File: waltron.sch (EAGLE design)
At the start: 21 parts, among them IC1 4049N, U1 LM386

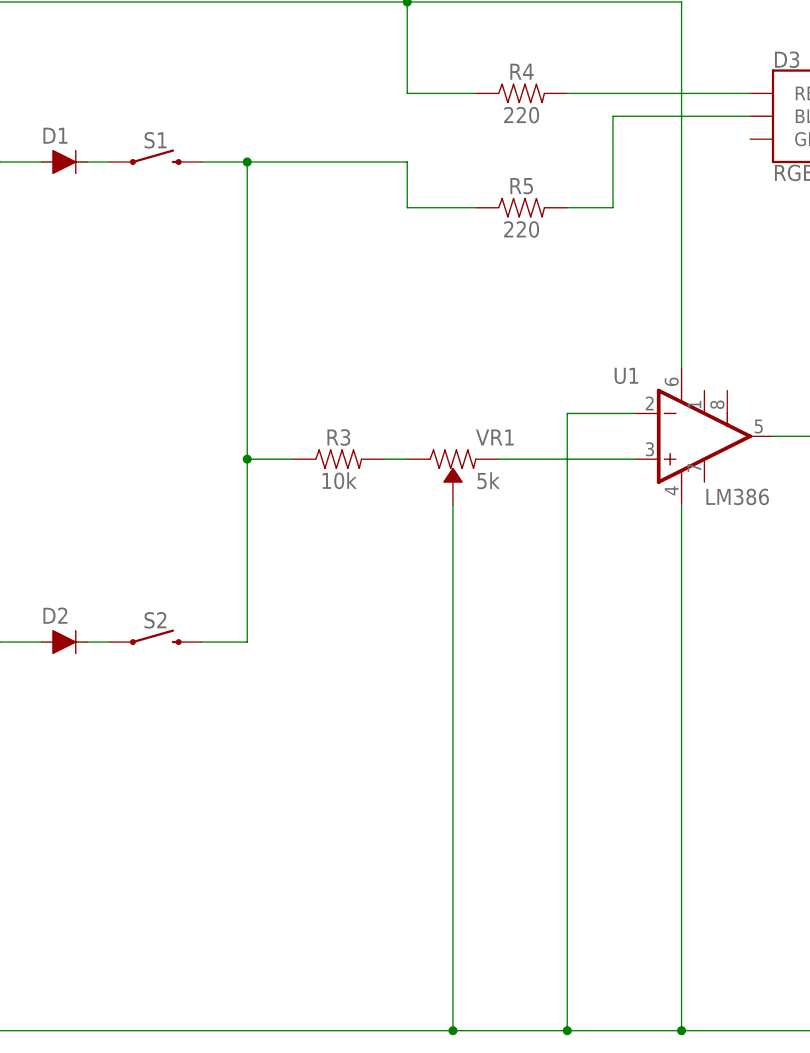
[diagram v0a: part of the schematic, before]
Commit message: Fix miswired volume pot
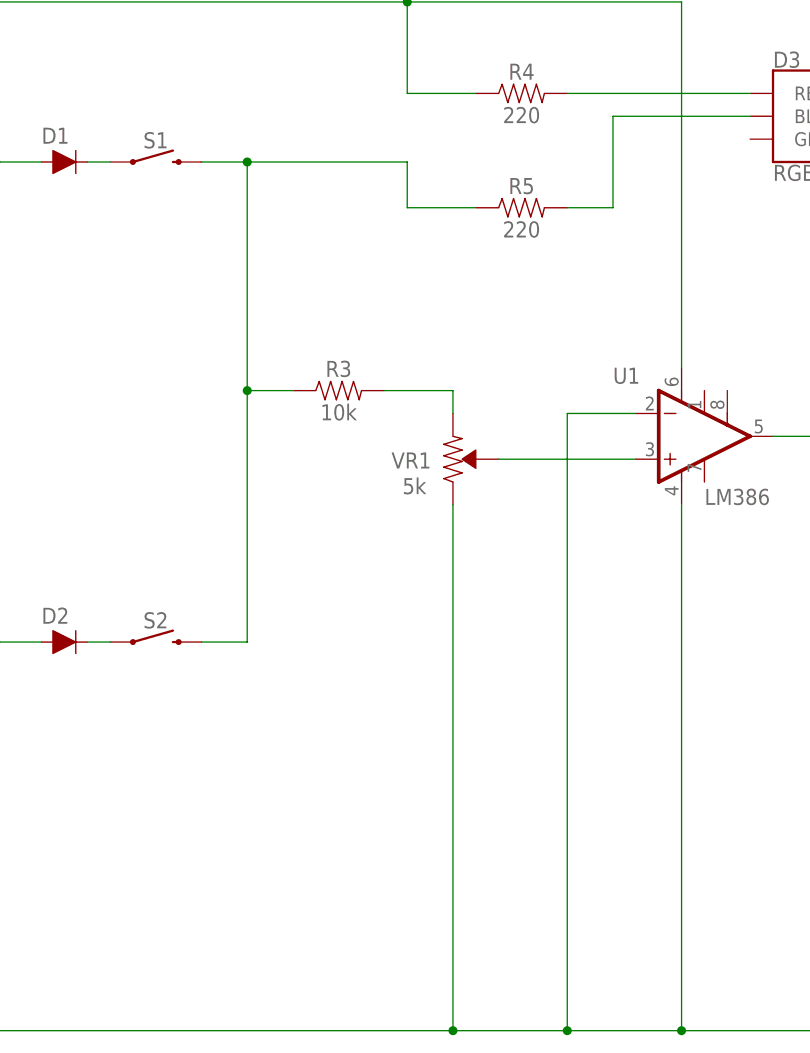
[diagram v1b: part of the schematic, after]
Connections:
- net GND: now also VR1.CW; no longer VR1.WIPER
- net N$13: now also R3.2; no longer U1.+IN
- net N$16: now also U1.+IN, VR1.WIPER; no longer R3.2, VR1.CW
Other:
- moved on the sheet: R3, VR1
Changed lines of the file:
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@@
 <attribute name="VALUE" x="104.14" y="14.732" size="1.778" layer="96" font="vector" align="top-center"/>
 </instance>
-<instance part="VR1" gate="R?" x="137.16" y="35.56" rot="R270"/>
+<instance part="VR1" gate="R?" x="137.16" y="35.56" smashed="yes">
+<attribute name="NAME" x="134.7417625" y="36.30701875" size="1.778" layer="95" font="vector" rot="R180"/>
+<attribute name="VALUE" x="134.206484375" y="31.675228125" size="1.778" layer="96" font="vector" rot="R180" align="top-left"/>
+</instance>
 <instance part="U1" gate="G1" x="162.56" y="38.1" smashed="yes">
 <attribute name="NAME" x="154.94" y="43.942" size="1.778" layer="95" font="vector"/>
@@
 <instance part="R5" gate="G$1" x="144.78" y="63.5"/>
 <instance part="R4" gate="G$1" x="144.78" y="76.2"/>
-<instance part="R3" gate="G$1" x="124.46" y="35.56"/>
+<instance part="R3" gate="G$1" x="124.46" y="43.18"/>
 <instance part="D1" gate="G$1" x="93.98" y="68.58"/>
 <instance part="D2" gate="G$1" x="93.98" y="15.24"/>
@@
 <net name="N$12" class="0">
 <segment>
-<wire x1="114.3" y1="68.58" x2="114.3" y2="35.56" width="0.1524" layer="91"/>
-<wire x1="114.3" y1="35.56" x2="114.3" y2="15.24" width="0.1524" layer="91"/>
+<wire x1="114.3" y1="68.58" x2="114.3" y2="43.18" width="0.1524" layer="91"/>
+<wire x1="114.3" y1="43.18" x2="114.3" y2="15.24" width="0.1524" layer="91"/>
 <pinref part="S1" gate="G$1" pin="2"/>
 <wire x1="109.22" y1="68.58" x2="114.3" y2="68.58" width="0.1524" layer="91"/>
@@
 <wire x1="109.22" y1="15.24" x2="114.3" y2="15.24" width="0.1524" layer="91"/>
 <pinref part="R3" gate="G$1" pin="1"/>
-<wire x1="119.38" y1="35.56" x2="114.3" y2="35.56" width="0.1524" layer="91"/>
-<junction x="114.3" y="35.56"/>
+<wire x1="119.38" y1="43.18" x2="114.3" y2="43.18" width="0.1524" layer="91"/>
+<junction x="114.3" y="43.18"/>
 <wire x1="114.3" y1="68.58" x2="132.08" y2="68.58" width="0.1524" layer="91"/>
 <junction x="114.3" y="68.58"/>
@@
 </segment>
 </net>
-<net name="N$13" class="0">
-<segment>
-<pinref part="VR1" gate="R?" pin="CCW"/>
-<pinref part="U1" gate="G1" pin="+IN"/>
-<wire x1="142.24" y1="35.56" x2="157.48" y2="35.56" width="0.1524" layer="91"/>
-</segment>
-</net>
 <net name="N$14" class="0">
 <segment>
@@
 <pinref part="S2" gate="G$1" pin="1"/>
 <wire x1="96.52" y1="15.24" x2="99.06" y2="15.24" width="0.1524" layer="91"/>
-</segment>
-</net>
-<net name="N$16" class="0">
-<segment>
-<pinref part="R3" gate="G$1" pin="2"/>
-<pinref part="VR1" gate="R?" pin="CW"/>
-<wire x1="129.54" y1="35.56" x2="132.08" y2="35.56" width="0.1524" layer="91"/>
 </segment>
 </net>
@@
 <net name="GND" class="1">
 <segment>
-<pinref part="VR1" gate="R?" pin="WIPER"/>
-<wire x1="137.16" y1="30.48" x2="137.16" y2="-27.94" width="0.1524" layer="91"/>
 <pinref part="U1" gate="G1" pin="-IN"/>
 <wire x1="157.48" y1="40.64" x2="149.86" y2="40.64" width="0.1524" layer="91"/>
 <wire x1="149.86" y1="40.64" x2="149.86" y2="-27.94" width="0.1524" layer="91"/>
-<wire x1="149.86" y1="-27.94" x2="137.16" y2="-27.94" width="0.1524" layer="91"/>
 <pinref part="U1" gate="G1" pin="V-"/>
 <wire x1="162.56" y1="30.48" x2="162.56" y2="-27.94" width="0.1524" layer="91"/>
@@
 <wire x1="-40.64" y1="35.56" x2="-40.64" y2="-27.94" width="0.1524" layer="91"/>
 <wire x1="-40.64" y1="-27.94" x2="-27.94" y2="-27.94" width="0.1524" layer="91"/>
-<junction x="137.16" y="-27.94"/>
 <wire x1="-27.94" y1="-27.94" x2="137.16" y2="-27.94" width="0.1524" layer="91"/>
+<wire x1="137.16" y1="-27.94" x2="149.86" y2="-27.94" width="0.1524" layer="91"/>
 <wire x1="-27.94" y1="27.94" x2="-27.94" y2="-27.94" width="0.1524" layer="91"/>
 <junction x="-27.94" y="-27.94"/>
@@
 <wire x1="-20.32" y1="33.02" x2="-20.32" y2="27.94" width="0.1524" layer="91"/>
 <wire x1="-20.32" y1="27.94" x2="-27.94" y2="27.94" width="0.1524" layer="91"/>
-</segment>
-</net>
+<pinref part="VR1" gate="R?" pin="CW"/>
+<wire x1="137.16" y1="30.48" x2="137.16" y2="-27.94" width="0.1524" layer="91"/>
+<junction x="137.16" y="-27.94"/>
+</segment>
+</net>
+<net name="N$13" class="0">
+<segment>
+<pinref part="R3" gate="G$1" pin="2"/>
+<wire x1="129.54" y1="43.18" x2="137.16" y2="43.18" width="0.1524" layer="91"/>
+<pinref part="VR1" gate="R?" pin="CCW"/>
+<wire x1="137.16" y1="43.18" x2="137.16" y2="40.64" width="0.1524" layer="91"/>
+</segment>
+</net>
+<net name="N$16" class="0">
+<segment>
+<pinref part="VR1" gate="R?" pin="WIPER"/>
+<pinref part="U1" gate="G1" pin="+IN"/>
+<wire x1="142.24" y1="35.56" x2="157.48" y2="35.56" width="0.1524" layer="91"/>
+</segment>
+</net>

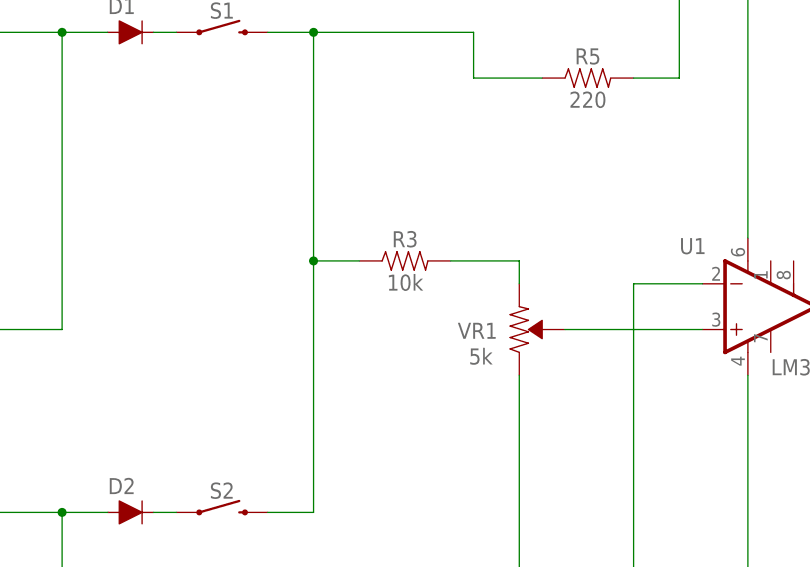
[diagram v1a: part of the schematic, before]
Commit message: Lay resistors flat, rip up routes
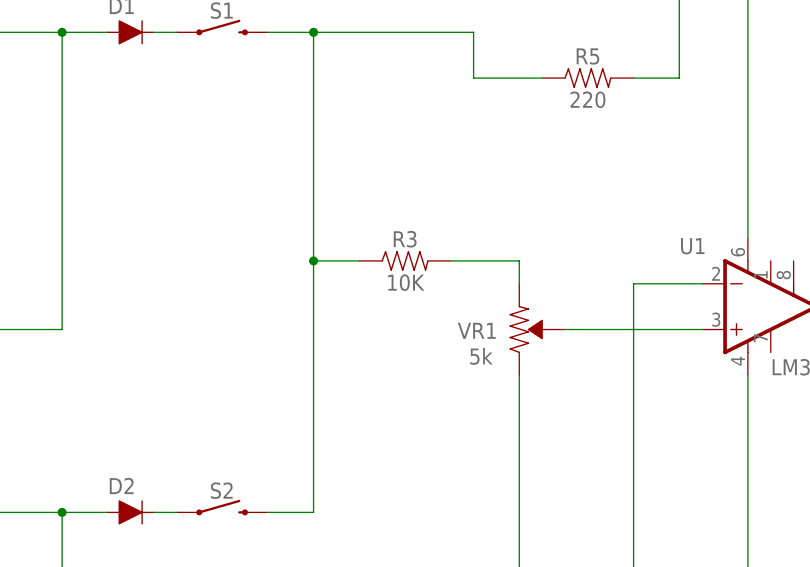
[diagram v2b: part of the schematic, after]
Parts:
- R1, R2, R4, R5: device SparkFun-Resistors:1MOHM-VERT-1/4W-5% -> SparkFun-Resistors:1KOHM-HORIZ-1/4W-1%
- R3: value 10k -> 10K; device SparkFun-Resistors:1MOHM-VERT-1/4W-5% -> SparkFun-Resistors:1KOHM-HORIZ-1/4W-1%
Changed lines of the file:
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@@
 <part name="PR1" library="SparkFun-Sensors" deviceset="PHOTOCELL" device="PTH-KIT" value=""/>
 <part name="C2" library="SparkFun-Capacitors" deviceset="10UF-POLAR" device="-RADIAL-2.5MM-25V-20%" value="4.7uF"/>
-<part name="R1" library="SparkFun-Resistors" deviceset="1MOHM" device="-VERT-1/4W-5%" value="1M"/>
+<part name="R1" library="SparkFun-Resistors" deviceset="1KOHM" device="-HORIZ-1/4W-1%" value="1M"/>
 <part name="S1" library="SparkFun-Switches" deviceset="MOMENTARY-SWITCH-SPST" device="-PTH-6.0MM" value=""/>
-<part name="R2" library="SparkFun-Resistors" deviceset="1MOHM" device="-VERT-1/4W-5%" value="1M"/>
+<part name="R2" library="SparkFun-Resistors" deviceset="1KOHM" device="-HORIZ-1/4W-1%" value="1M"/>
 <part name="C1" library="SparkFun-Capacitors" deviceset="0.1UF" device="-KIT-EZ-50V-20%" value="0.1uF"/>
 <part name="PR2" library="SparkFun-Sensors" deviceset="PHOTOCELL" device="PTH-KIT" value=""/>
@@
 <part name="SPEAKER" library="SparkFun-Connectors" deviceset="CONN_02" device="" value="8ohm"/>
 <part name="D3" library="SparkFun-LED" deviceset="LED-RGB-CC" device="CLEAR" value="RGB LED"/>
-<part name="R5" library="SparkFun-Resistors" deviceset="1MOHM" device="-VERT-1/4W-5%" value="220"/>
-<part name="R4" library="SparkFun-Resistors" deviceset="1MOHM" device="-VERT-1/4W-5%" value="220"/>
-<part name="R3" library="SparkFun-Resistors" deviceset="1MOHM" device="-VERT-1/4W-5%" value="10k"/>
+<part name="R5" library="SparkFun-Resistors" deviceset="1KOHM" device="-HORIZ-1/4W-1%" value="220"/>
+<part name="R4" library="SparkFun-Resistors" deviceset="1KOHM" device="-HORIZ-1/4W-1%" value="220"/>
+<part name="R3" library="SparkFun-Resistors" deviceset="1KOHM" device="-HORIZ-1/4W-1%" value="10K"/>
 <part name="D1" library="SparkFun-DiscreteSemi" deviceset="DIODE" device="-1N4148" value=""/>
 <part name="D2" library="SparkFun-DiscreteSemi" deviceset="DIODE" device="-1N4148" value=""/>

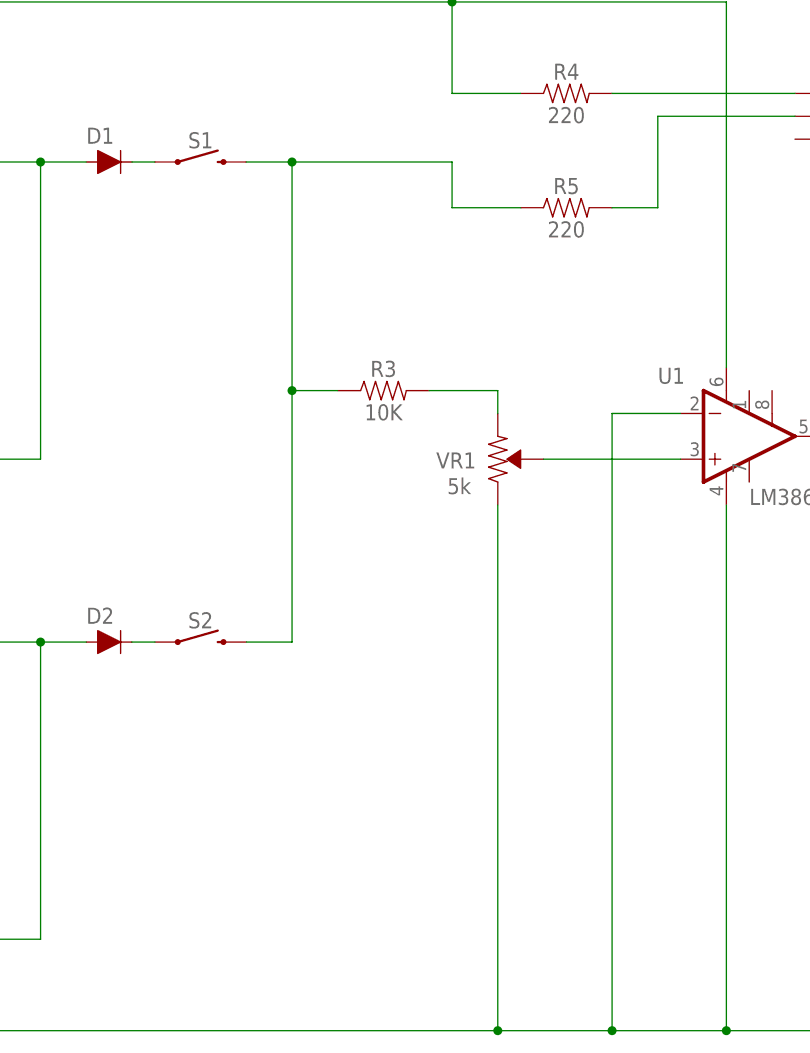
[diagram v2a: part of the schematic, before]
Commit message: Switch out trimmer
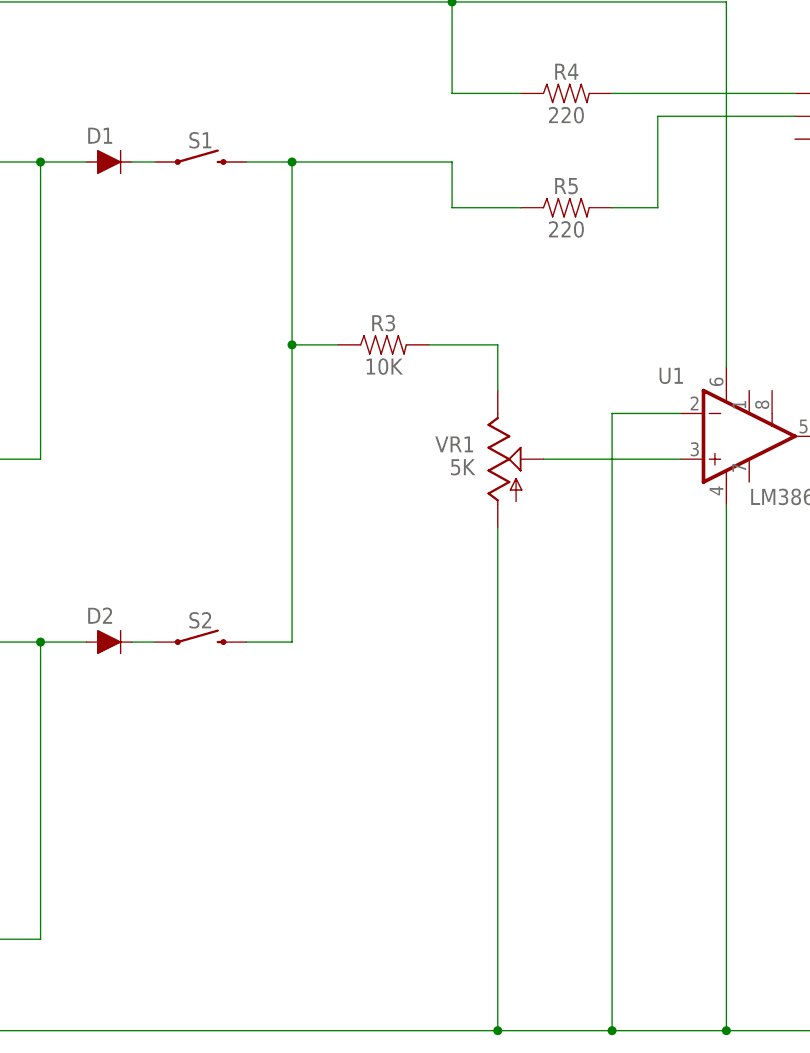
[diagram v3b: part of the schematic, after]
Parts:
- VR1: value 5k -> 5K; device SparkFun-Resistors:TRIMPOT-PTH-10MM-KNOB-1/2W-10% -> adafruit:TRIM
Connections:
- net GND: now also VR1.A; no longer VR1.CW
- net N$13: now also VR1.E; no longer VR1.CCW
- net N$16: now also VR1.S; no longer VR1.WIPER
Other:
- moved on the sheet: R3
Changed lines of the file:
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@@
 <layer number="230" name="230bmp" color="7" fill="1" visible="yes" active="yes"/>
 <layer number="231" name="231bmp" color="7" fill="1" visible="yes" active="yes"/>
+<layer number="232" name="Eagle3D_PG2" color="7" fill="1" visible="no" active="no"/>
+<layer number="233" name="Eagle3D_PG3" color="7" fill="1" visible="no" active="no"/>
 <layer number="248" name="Housing" color="7" fill="1" visible="yes" active="yes"/>
 <layer number="249" name="Edge" color="7" fill="1" visible="yes" active="yes"/>
@@
 <part name="PR3" library="SparkFun-Sensors" deviceset="PHOTOCELL" device="PTH-KIT" value=""/>
 <part name="S2" library="SparkFun-Switches" deviceset="MOMENTARY-SWITCH-SPST" device="-PTH-6.0MM" value=""/>
-<part name="VR1" library="SparkFun-Resistors" deviceset="TRIMPOT" device="-PTH-10MM-KNOB-1/2W-10%" value="5k"/>
 <part name="U1" library="SparkFun-IC-Amplifiers" deviceset="LM386" device="" value="LM386"/>
 <part name="C3" library="SparkFun-Capacitors" deviceset="10UF-POLAR" device="-RADIAL-2.5MM-25V-20%" value="47uF"/>
@@
 <part name="P+1" library="supply1" deviceset="V+" device=""/>
 <part name="GND1" library="supply1" deviceset="GND" device=""/>
+<part name="VR1" library="adafruit" deviceset="TRIM" device="" value="5K"/>
 </parts>
 <sheets>
@@
 <attribute name="VALUE" x="104.14" y="14.732" size="1.778" layer="96" font="vector" align="top-center"/>
 </instance>
-<instance part="VR1" gate="R?" x="137.16" y="35.56" smashed="yes">
-<attribute name="NAME" x="134.7417625" y="36.30701875" size="1.778" layer="95" font="vector" rot="R180"/>
-<attribute name="VALUE" x="134.206484375" y="31.675228125" size="1.778" layer="96" font="vector" rot="R180" align="top-left"/>
-</instance>
 <instance part="U1" gate="G1" x="162.56" y="38.1" smashed="yes">
 <attribute name="NAME" x="154.94" y="43.942" size="1.778" layer="95" font="vector"/>
@@
 <instance part="R5" gate="G$1" x="144.78" y="63.5"/>
 <instance part="R4" gate="G$1" x="144.78" y="76.2"/>
-<instance part="R3" gate="G$1" x="124.46" y="43.18"/>
+<instance part="R3" gate="G$1" x="124.46" y="48.26"/>
 <instance part="D1" gate="G$1" x="93.98" y="68.58"/>
 <instance part="D2" gate="G$1" x="93.98" y="15.24"/>
 <instance part="P+1" gate="1" x="-45.72" y="66.04"/>
 <instance part="GND1" gate="1" x="-45.72" y="30.48"/>
+<instance part="VR1" gate="G$1" x="137.16" y="35.56" smashed="yes">
+<attribute name="NAME" x="134.62" y="38.1" size="1.778" layer="95" rot="R180"/>
+<attribute name="VALUE" x="134.62" y="35.56" size="1.778" layer="96" rot="R180"/>
+</instance>
 </instances>
 <busses>
@@
 <net name="N$12" class="0">
 <segment>
-<wire x1="114.3" y1="68.58" x2="114.3" y2="43.18" width="0.1524" layer="91"/>
-<wire x1="114.3" y1="43.18" x2="114.3" y2="15.24" width="0.1524" layer="91"/>
+<wire x1="114.3" y1="68.58" x2="114.3" y2="48.26" width="0.1524" layer="91"/>
+<wire x1="114.3" y1="48.26" x2="114.3" y2="15.24" width="0.1524" layer="91"/>
 <pinref part="S1" gate="G$1" pin="2"/>
 <wire x1="109.22" y1="68.58" x2="114.3" y2="68.58" width="0.1524" layer="91"/>
@@
 <wire x1="109.22" y1="15.24" x2="114.3" y2="15.24" width="0.1524" layer="91"/>
 <pinref part="R3" gate="G$1" pin="1"/>
-<wire x1="119.38" y1="43.18" x2="114.3" y2="43.18" width="0.1524" layer="91"/>
-<junction x="114.3" y="43.18"/>
+<wire x1="119.38" y1="48.26" x2="114.3" y2="48.26" width="0.1524" layer="91"/>
+<junction x="114.3" y="48.26"/>
 <wire x1="114.3" y1="68.58" x2="132.08" y2="68.58" width="0.1524" layer="91"/>
 <junction x="114.3" y="68.58"/>
@@
 <wire x1="-20.32" y1="33.02" x2="-20.32" y2="27.94" width="0.1524" layer="91"/>
 <wire x1="-20.32" y1="27.94" x2="-27.94" y2="27.94" width="0.1524" layer="91"/>
-<pinref part="VR1" gate="R?" pin="CW"/>
-<wire x1="137.16" y1="30.48" x2="137.16" y2="-27.94" width="0.1524" layer="91"/>
+<pinref part="VR1" gate="G$1" pin="A"/>
+<wire x1="137.16" y1="27.94" x2="137.16" y2="-27.94" width="0.1524" layer="91"/>
 <junction x="137.16" y="-27.94"/>
 </segment>
@@
 <segment>
 <pinref part="R3" gate="G$1" pin="2"/>
-<wire x1="129.54" y1="43.18" x2="137.16" y2="43.18" width="0.1524" layer="91"/>
-<pinref part="VR1" gate="R?" pin="CCW"/>
-<wire x1="137.16" y1="43.18" x2="137.16" y2="40.64" width="0.1524" layer="91"/>
+<wire x1="129.54" y1="48.26" x2="137.16" y2="48.26" width="0.1524" layer="91"/>
+<pinref part="VR1" gate="G$1" pin="E"/>
+<wire x1="137.16" y1="43.18" x2="137.16" y2="48.26" width="0.1524" layer="91"/>
 </segment>
 </net>
 <net name="N$16" class="0">
 <segment>
-<pinref part="VR1" gate="R?" pin="WIPER"/>
+<pinref part="VR1" gate="G$1" pin="S"/>
 <pinref part="U1" gate="G1" pin="+IN"/>
 <wire x1="142.24" y1="35.56" x2="157.48" y2="35.56" width="0.1524" layer="91"/>
